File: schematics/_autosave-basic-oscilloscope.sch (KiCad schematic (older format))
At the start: 64 parts, among them J1 9V_BATTERY, J2 12V_DC_JACK, J3 CH1, J4 CH2, SW1 SW_Push, SW2 SW_Push, SW3 SW_Push, SW4 SW_Push, SW5 SW_SPST, SW6 SW_Push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

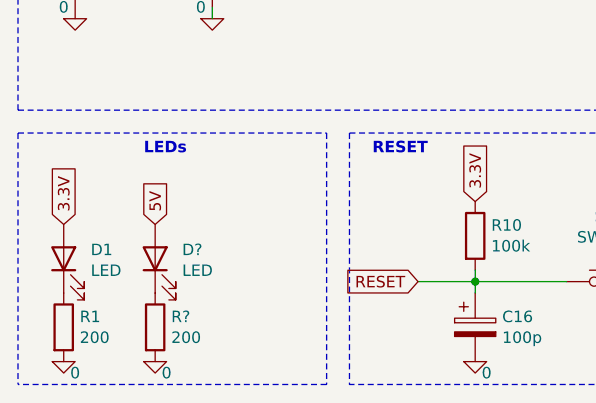
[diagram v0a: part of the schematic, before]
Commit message: create pcb layout
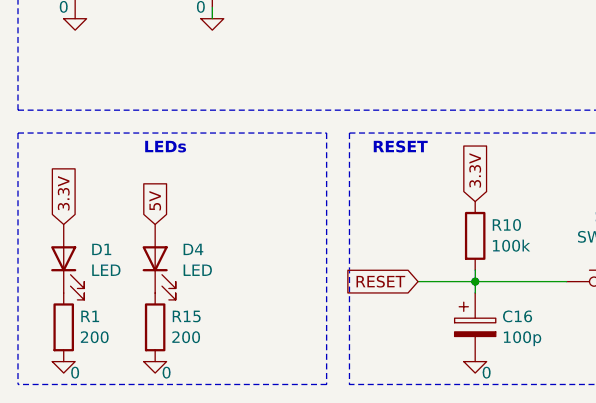
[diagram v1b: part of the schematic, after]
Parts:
- D1: footprint (none) -> Diode_SMD:D_0603_1608Metric
- D4: renamed from D?; footprint (none) -> Diode_SMD:D_0603_1608Metric
- R1: footprint (none) -> Resistor_SMD:R_0603_1608Metric
- R15: renamed from R?; footprint (none) -> Resistor_SMD:R_0603_1608Metric
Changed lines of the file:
@@
 F 0 "D1" V 839 7032 50  0000 R CNN
 F 1 "LED" V 748 7032 50  0000 R CNN
-F 2 "" H 800 7150 50  0001 C CNN
+F 2 "Diode_SMD:D_0603_1608Metric" H 800 7150 50  0001 C CNN
 F 3 "~" H 800 7150 50  0001 C CNN
 	1    800  7150
@@
 F 0 "R1" H 870 7496 50  0000 L CNN
 F 1 "200" H 870 7405 50  0000 L CNN
-F 2 "" V 730 7450 50  0001 C CNN
+F 2 "Resistor_SMD:R_0603_1608Metric" V 730 7450 50  0001 C CNN
 F 3 "~" H 800 7450 50  0001 C CNN
 	1    800  7450
@@
 5V
 $Comp
-L Device:LED D?
+L Device:LED D4
 U 1 1 611B9DB8
 P 1200 7150
-F 0 "D?" V 1239 7032 50  0000 R CNN
+F 0 "D4" V 1239 7032 50  0000 R CNN
 F 1 "LED" V 1148 7032 50  0000 R CNN
-F 2 "" H 1200 7150 50  0001 C CNN
+F 2 "Diode_SMD:D_0603_1608Metric" H 1200 7150 50  0001 C CNN
 F 3 "~" H 1200 7150 50  0001 C CNN
 	1    1200 7150
@@
 $EndComp
 $Comp
-L Device:R R?
+L Device:R R15
 U 1 1 611BA400
 P 1200 7450
-F 0 "R?" H 1270 7496 50  0000 L CNN
+F 0 "R15" H 1270 7496 50  0000 L CNN
 F 1 "200" H 1270 7405 50  0000 L CNN
-F 2 "" V 1130 7450 50  0001 C CNN
+F 2 "Resistor_SMD:R_0603_1608Metric" V 1130 7450 50  0001 C CNN
 F 3 "~" H 1200 7450 50  0001 C CNN
 	1    1200 7450
@@
 $EndComp
 $Comp
-L pspice:0 #GND?
+L pspice:0 #GND0101
 U 1 1 611BA7E8
 P 1200 7600
-F 0 "#GND?" H 1200 7500 50  0001 C CNN
+F 0 "#GND0101" H 1200 7500 50  0001 C CNN
 F 1 "0" H 1250 7550 50  0000 C CNN
 F 2 "" H 1200 7600 50  0001 C CNN
